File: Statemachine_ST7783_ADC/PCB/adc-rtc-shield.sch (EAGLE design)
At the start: 56 parts, among them IC1 TLC2543, IC2 RV_3049_C2, J10 MC1,5/2-G-3,5, J11 MC1,5/2-G-3,5, J12 MC1,5/2-G-3,5, J13 MC1,5/2-G-3,5, J14 MC1,5/2-G-3,5, J15 MC1,5/2-G-3,5, J16 MC1,5/2-G-3,5, J9 MC1,5/2-G-3,5

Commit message: edit board.
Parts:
- removed J10, J11, J12, J13, J14, J15, J16, J9: MC1,5/2-G-3,5, PHOENIX:MC1,5/2-G-3,5
- added JP1: 9x1F-H8.5, pinhead:PINHD-1X9/90
- added JP2, JP3, JP4, JP5, JP6, JP7: (no value), pinhead:PINHD-1X1
- C27: device rcl:C-EUC0402S -> rcl:C-EUC0603
- R10, R13, R14, R15, R16, R17, R4, R5, R6, R8, R9: device Passiv:R@2 -> resistor:R-EU_0207/10
- R11, R12, R18, R19, R2, R20, R21, R3, R7: device Passiv:R@2 -> resistor:R-EU_0207/12
- R22: device rcl:R-EU_R0603 -> rcl:R-EU_0207/10
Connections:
- removed net N$26: IC2.CS
- removed net N$27: BATT2.+, R22.1
- new net +BAT: BATT2.+, JP4.1, JP5.1, R22.1
- new net AD4/SDA': AD.5
- new net AD5/SCL': AD.6
- net +5V: now also JP6.1, JP7.1; no longer POWER.2
- net AD4/SDA: now also IC2.CS; no longer AD.5, IC1./CS
- net AD5/SCL: now also IC1./CS; no longer AD.6
- net GND: now also JP1.1, JP2.1, JP3.1; no longer J10.2.1, J11.2.1, J12.2.1, J13.2.1, J14.2.1, J15.2.1, J16.2.1, J9.2.1
- net X1_RX4-: now also JP1.9; no longer J9.1.1
- net X2_TX4-: now also JP1.8; no longer J10.1.1
- net X3_RX3-: now also JP1.7; no longer J11.1.1
- net X4_TX3-: now also JP1.6; no longer J12.1.1
- net X5_RX2-: now also JP1.5; no longer J13.1.1
- net X6_TX2-: now also JP1.4; no longer J14.1.1
- net X7_RX1-: now also JP1.3; no longer J15.1.1
- net X8_TX1-: now also JP1.2; no longer J16.1.1

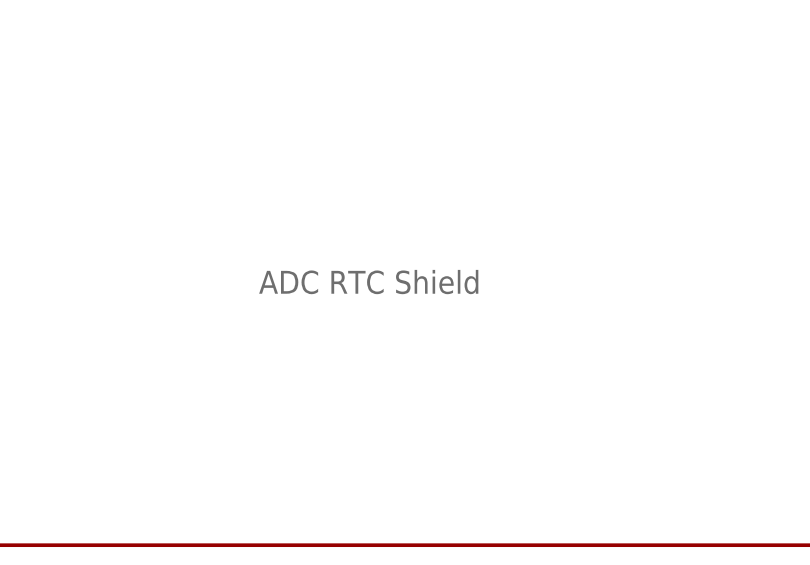
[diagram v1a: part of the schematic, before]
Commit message: Remove Arduino text.
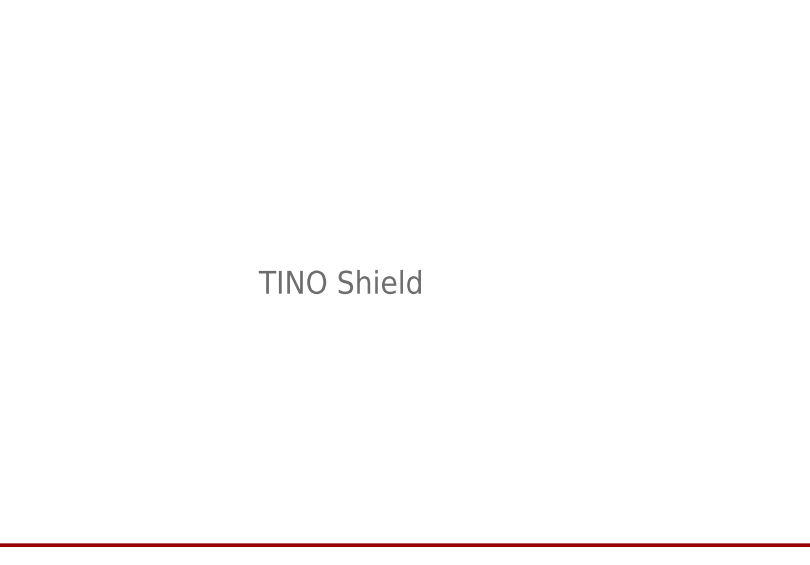
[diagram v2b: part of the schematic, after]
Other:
- note added: "TINO Shield"
- note removed: "ADC RTC Shield"
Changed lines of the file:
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@@
 <grid distance="0.1" unitdist="inch" unit="inch" style="lines" multiple="1" display="no" altdistance="0.01" altunitdist="inch" altunit="inch"/>
 <layers>
-<layer number="1" name="Top" color="4" fill="1" visible="yes" active="no"/>
-<layer number="2" name="Route2" color="1" fill="3" visible="yes" active="no"/>
-<layer number="3" name="Route3" color="4" fill="3" visible="yes" active="no"/>
-<layer number="4" name="Route4" color="1" fill="4" visible="yes" active="no"/>
-<layer number="5" name="Route5" color="4" fill="4" visible="yes" active="no"/>
-<layer number="6" name="Route6" color="1" fill="8" visible="yes" active="no"/>
-<layer number="7" name="Route7" color="4" fill="8" visible="yes" active="no"/>
-<layer number="8" name="Route8" color="1" fill="2" visible="yes" active="no"/>
-<layer number="9" name="Route9" color="4" fill="2" visible="yes" active="no"/>
-<layer number="10" name="Route10" color="1" fill="7" visible="yes" active="no"/>
-<layer number="11" name="Route11" color="4" fill="7" visible="yes" active="no"/>
-<layer number="12" name="Route12" color="1" fill="5" visible="yes" active="no"/>
-<layer number="13" name="Route13" color="4" fill="5" visible="yes" active="no"/>
-<layer number="14" name="Route14" color="1" fill="6" visible="yes" active="no"/>
-<layer number="15" name="Route15" color="4" fill="6" visible="yes" active="no"/>
-<layer number="16" name="Bottom" color="1" fill="1" visible="yes" active="no"/>
-<layer number="17" name="Pads" color="2" fill="1" visible="yes" active="no"/>
-<layer number="18" name="Vias" color="14" fill="1" visible="yes" active="no"/>
-<layer number="19" name="Unrouted" color="6" fill="1" visible="yes" active="no"/>
-<layer number="20" name="Dimension" color="15" fill="1" visible="yes" active="no"/>
-<layer number="21" name="tPlace" color="7" fill="1" visible="yes" active="no"/>
-<layer number="22" name="bPlace" color="7" fill="1" visible="yes" active="no"/>
-<layer number="23" name="tOrigins" color="15" fill="1" visible="yes" active="no"/>
-<layer number="24" name="bOrigins" color="15" fill="1" visible="yes" active="no"/>
-<layer number="25" name="tNames" color="7" fill="1" visible="yes" active="no"/>
-<layer number="26" name="bNames" color="7" fill="1" visible="yes" active="no"/>
-<layer number="27" name="tValues" color="7" fill="1" visible="yes" active="no"/>
-<layer number="28" name="bValues" color="7" fill="1" visible="yes" active="no"/>
+<layer number="1" name="Top" color="4" fill="1" visible="no" active="no"/>
+<layer number="2" name="Route2" color="1" fill="3" visible="no" active="no"/>
+<layer number="3" name="Route3" color="4" fill="3" visible="no" active="no"/>
+<layer number="4" name="Route4" color="1" fill="4" visible="no" active="no"/>
+<layer number="5" name="Route5" color="4" fill="4" visible="no" active="no"/>
+<layer number="6" name="Route6" color="1" fill="8" visible="no" active="no"/>
+<layer number="7" name="Route7" color="4" fill="8" visible="no" active="no"/>
+<layer number="8" name="Route8" color="1" fill="2" visible="no" active="no"/>
+<layer number="9" name="Route9" color="4" fill="2" visible="no" active="no"/>
+<layer number="10" name="Route10" color="1" fill="7" visible="no" active="no"/>
+<layer number="11" name="Route11" color="4" fill="7" visible="no" active="no"/>
+<layer number="12" name="Route12" color="1" fill="5" visible="no" active="no"/>
+<layer number="13" name="Route13" color="4" fill="5" visible="no" active="no"/>
+<layer number="14" name="Route14" color="1" fill="6" visible="no" active="no"/>
+<layer number="15" name="Route15" color="4" fill="6" visible="no" active="no"/>
+<layer number="16" name="Bottom" color="1" fill="1" visible="no" active="no"/>
+<layer number="17" name="Pads" color="2" fill="1" visible="no" active="no"/>
+<layer number="18" name="Vias" color="14" fill="1" visible="no" active="no"/>
+<layer number="19" name="Unrouted" color="6" fill="1" visible="no" active="no"/>
+<layer number="20" name="Dimension" color="15" fill="1" visible="no" active="no"/>
+<layer number="21" name="tPlace" color="7" fill="1" visible="no" active="no"/>
+<layer number="22" name="bPlace" color="7" fill="1" visible="no" active="no"/>
+<layer number="23" name="tOrigins" color="15" fill="1" visible="no" active="no"/>
+<layer number="24" name="bOrigins" color="15" fill="1" visible="no" active="no"/>
+<layer number="25" name="tNames" color="7" fill="1" visible="no" active="no"/>
+<layer number="26" name="bNames" color="7" fill="1" visible="no" active="no"/>
+<layer number="27" name="tValues" color="7" fill="1" visible="no" active="no"/>
+<layer number="28" name="bValues" color="7" fill="1" visible="no" active="no"/>
 <layer number="29" name="tStop" color="2" fill="3" visible="no" active="no"/>
 <layer number="30" name="bStop" color="5" fill="6" visible="no" active="no"/>
@@
 <layer number="35" name="tGlue" color="7" fill="4" visible="no" active="no"/>
 <layer number="36" name="bGlue" color="7" fill="5" visible="no" active="no"/>
-<layer number="37" name="tTest" color="7" fill="1" visible="yes" active="no"/>
-<layer number="38" name="bTest" color="7" fill="1" visible="yes" active="no"/>
+<layer number="37" name="tTest" color="7" fill="1" visible="no" active="no"/>
+<layer number="38" name="bTest" color="7" fill="1" visible="no" active="no"/>
 <layer number="39" name="tKeepout" color="4" fill="11" visible="no" active="no"/>
 <layer number="40" name="bKeepout" color="1" fill="11" visible="no" active="no"/>
@@
 <layer number="44" name="Drills" color="7" fill="1" visible="no" active="no"/>
 <layer number="45" name="Holes" color="7" fill="1" visible="no" active="no"/>
-<layer number="46" name="Milling" color="3" fill="1" visible="yes" active="no"/>
-<layer number="47" name="Measures" color="12" fill="1" visible="yes" active="no"/>
-<layer number="48" name="Document" color="7" fill="1" visible="yes" active="no"/>
-<layer number="49" name="Reference" color="13" fill="1" visible="yes" active="no"/>
-<layer number="50" name="dxf" color="12" fill="1" visible="yes" active="no"/>
-<layer number="51" name="tDocu" color="7" fill="1" visible="yes" active="no"/>
-<layer number="52" name="bDocu" color="7" fill="1" visible="yes" active="no"/>
-<layer number="53" name="tGND_GNDA" color="7" fill="1" visible="yes" active="no"/>
-<layer number="54" name="bGND_GNDA" color="7" fill="1" visible="yes" active="no"/>
-<layer number="56" name="wert" color="7" fill="1" visible="yes" active="no"/>
+<layer number="46" name="Milling" color="3" fill="1" visible="no" active="no"/>
+<layer number="47" name="Measures" color="12" fill="1" visible="no" active="no"/>
+<layer number="48" name="Document" color="7" fill="1" visible="no" active="no"/>
+<layer number="49" name="Reference" color="13" fill="1" visible="no" active="no"/>
+<layer number="50" name="dxf" color="12" fill="1" visible="no" active="no"/>
+<layer number="51" name="tDocu" color="7" fill="1" visible="no" active="no"/>
+<layer number="52" name="bDocu" color="7" fill="1" visible="no" active="no"/>
+<layer number="53" name="tGND_GNDA" color="7" fill="1" visible="no" active="no"/>
+<layer number="54" name="bGND_GNDA" color="7" fill="1" visible="no" active="no"/>
+<layer number="56" name="wert" color="7" fill="1" visible="no" active="no"/>
 <layer number="91" name="Nets" color="2" fill="1" visible="yes" active="yes"/>
 <layer number="92" name="Busses" color="1" fill="1" visible="yes" active="yes"/>
@@
 <text x="332.74" y="147.32" size="1.778" layer="91">SDA</text>
 <text x="332.74" y="149.86" size="1.778" layer="91">SCL</text>
-<text x="309.88" y="27.94" size="2.54" layer="95">ADC RTC Shield</text>
+<text x="309.88" y="27.94" size="2.54" layer="95">TINO Shield</text>
 <text x="337.82" y="101.6" size="1.778" layer="91">Achtung!
 --------------------------------------------------

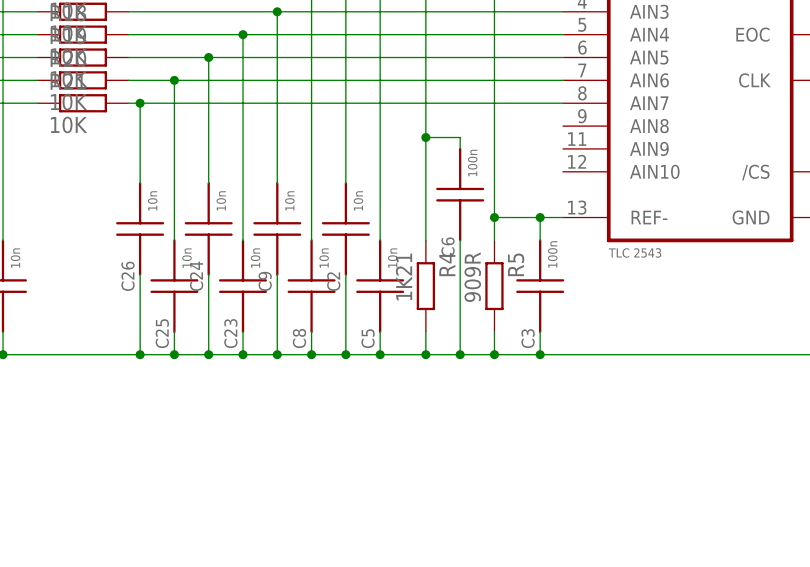
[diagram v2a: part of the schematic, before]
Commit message: Voltage devider changed.
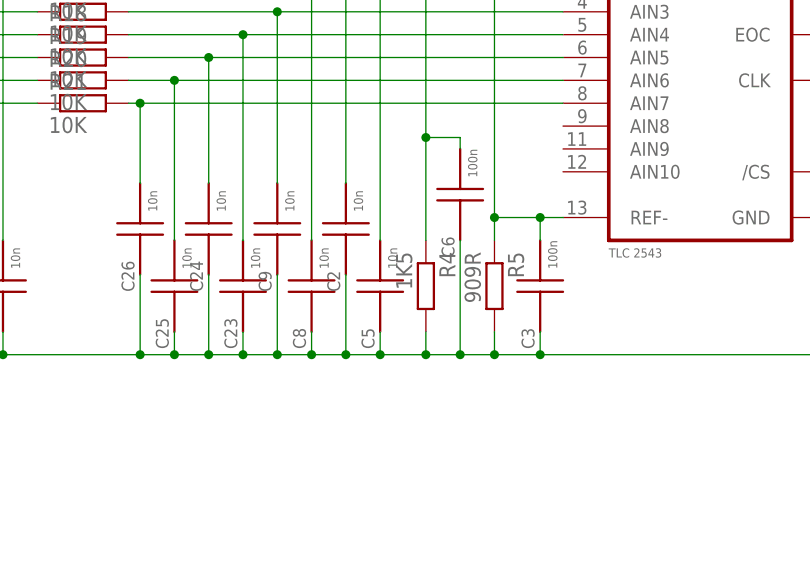
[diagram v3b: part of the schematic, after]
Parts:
- R4: value 1K21 -> 1K5
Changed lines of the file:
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@@
 <part name="R2" library="resistor" deviceset="R-EU_" device="0207/12" value="10K"/>
 <part name="R3" library="resistor" deviceset="R-EU_" device="0207/12" value="10K"/>
-<part name="R4" library="resistor" deviceset="R-EU_" device="0207/10" value="1K21"/>
+<part name="R4" library="resistor" deviceset="R-EU_" device="0207/10" value="1K5"/>
 <part name="R5" library="resistor" deviceset="R-EU_" device="0207/10" value="909R"/>
 <part name="R6" library="resistor" deviceset="R-EU_" device="0207/10" value="2K"/>
